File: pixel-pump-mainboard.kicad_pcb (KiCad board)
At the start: 4 copper layers, 68 x 67.3 mm, 134 parts, among them J1 JST NC Valve, J10 BM10B-SRSS-TB(LF)(SN), J11 UART/SWD DNP, J12 TYPE-C-31-M-12, J2 JST NO Valve, J3 6P4C, J4 JST 3 Way Valve, J5 Jack-DC 12V, J6 Power Sw, J7 EXP1, J8 EXP2, J9 BM04B-SRSS-TBT(LF)(SN), Q1 BSS138, Q2 BSS138, Q3 BSS138, Q4 STN4NF20L, Q5 BSS138, SW1 BOOTSEL, U1 LD1117S33TR, U2 TPS62112RSAR, U3 W25Q128JVPIQ, U4 RP2040, Y1 ABMM2-12.000MHZ-E2-T

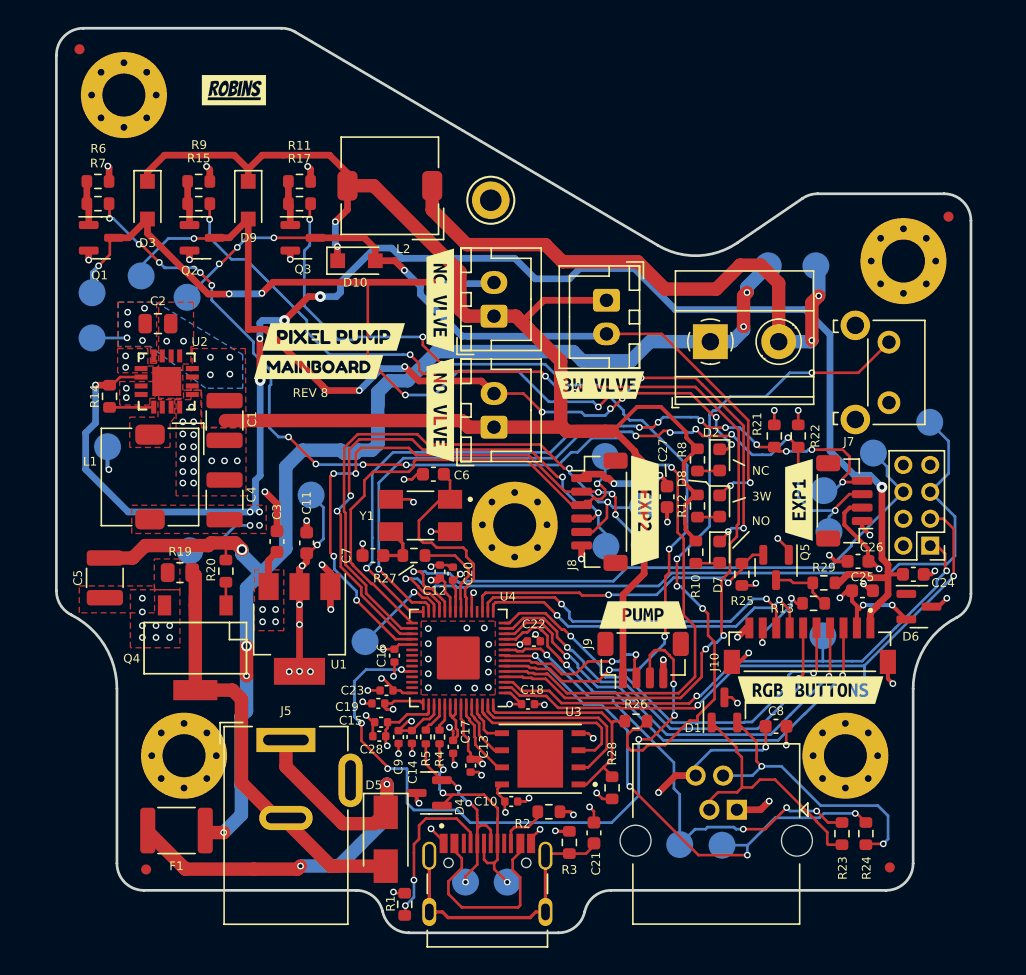
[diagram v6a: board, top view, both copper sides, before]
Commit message: Add Aisler Bridge marks
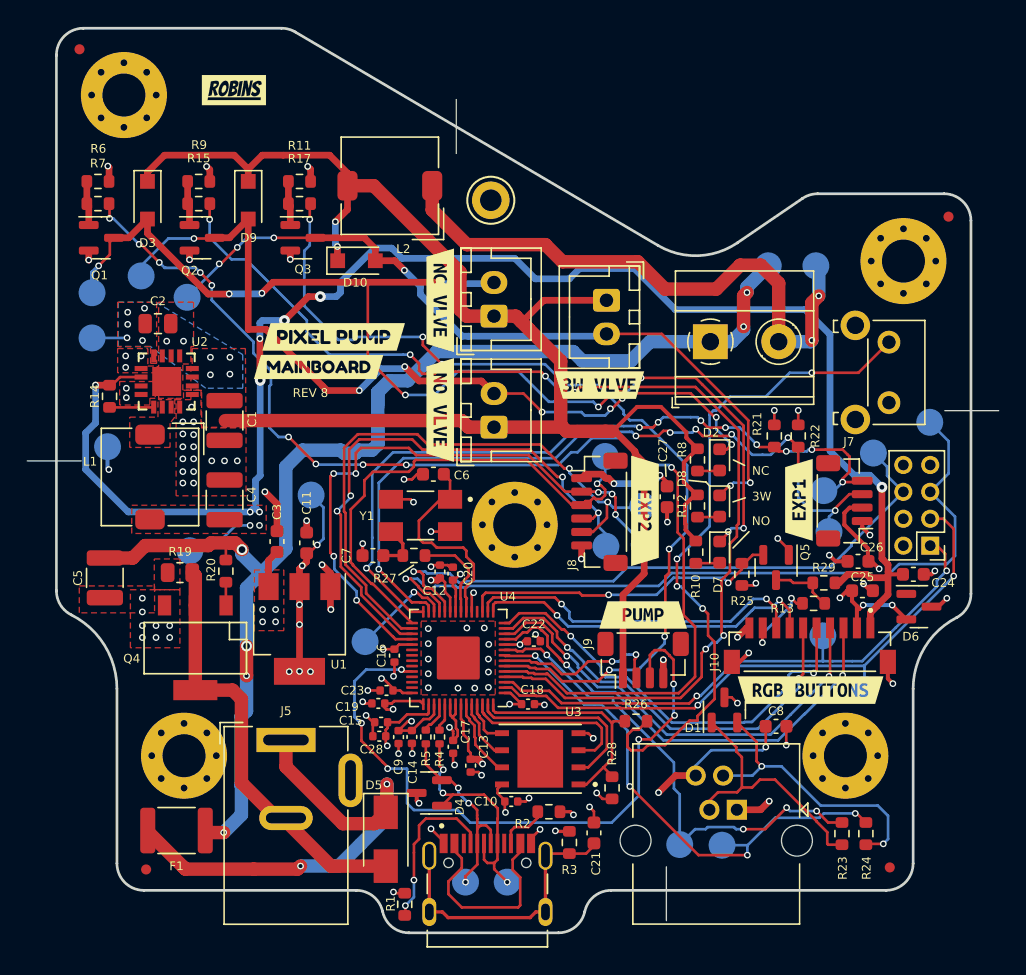
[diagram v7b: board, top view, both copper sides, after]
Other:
- board size 68 x 67.3 mm -> 72.2 x 67.3 mm
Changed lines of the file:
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@@
   (gr_line (start 92.210564 157.59322) (end 103.329656 157.59322) (layer "Edge.Cuts") (width 0.2))
   (gr_arc (start 82.739452 90.3336) (mid 83.265052 90.403899) (end 83.753702 90.609855) (layer "Edge.Cuts") (width 0.2))
+  (gr_line (start 63.8302 122.5042) (end 67.8434 122.5042) (layer "Edge.Cuts") (width 0.05))
   (gr_arc (start 121.475992 102.987506) (mid 122.013008 102.728973) (end 122.602363 102.640167) (layer "Edge.Cuts") (width 0.2))
   (gr_arc (start 72.5 154.434856) (mid 71.085786 153.84907) (end 70.5 152.434856) (layer "Edge.Cuts") (width 0.2))
@@
   (gr_line (start 132 102.640167) (end 122.602363 102.640167) (layer "Edge.Cuts") (width 0.2))
   (gr_arc (start 105.284883 156.014038) (mid 105.983455 154.878958) (end 107.24011 154.434856) (layer "Edge.Cuts") (width 0.2))
+  (gr_line (start 95.7326 99.6442) (end 95.7326 95.631) (layer "Edge.Cuts") (width 0.05))
   (gr_line (start 72.5 154.434856) (end 88.30011 154.434856) (layer "Edge.Cuts") (width 0.2))
   (gr_arc (start 134 132.387559) (mid 133.708285 133.427636) (end 132.918238 134.164307) (layer "Edge.Cuts") (width 0.2))
   (gr_arc (start 92.210564 157.59322) (mid 90.953909 157.149118) (end 90.255337 156.014038) (layer "Edge.Cuts") (width 0.2))
   (gr_arc (start 67.104294 133.951376) (mid 66.298322 133.214015) (end 66 132.163161) (layer "Edge.Cuts") (width 0.2))
+  (gr_line (start 111.3536 156.6926) (end 111.3536 152.6794) (layer "Edge.Cuts") (width 0.05))
   (gr_line (start 134 132.387558) (end 134 104.640167) (layer "Edge.Cuts") (width 0.2))
   (gr_arc (start 116.62628 106.292828) (mid 113.711299 107.244981) (end 110.739573 106.48831) (layer "Edge.Cuts") (width 0.2))
@@
   (gr_line (start 82.739452 90.333601) (end 68 90.333601) (layer "Edge.Cuts") (width 0.2))
   (gr_line (start 110.739573 106.48831) (end 83.753702 90.609855) (layer "Edge.Cuts") (width 0.2))
+  (gr_line (start 132.0546 118.7704) (end 136.0678 118.7704) (layer "Edge.Cuts") (width 0.05))
   (gr_arc (start 67.104294 133.951375) (mid 69.582658 136.218759) (end 70.5 139.450136) (layer "Edge.Cuts") (width 0.2))
   (gr_arc (start 129.699999 152.434855) (mid 129.114213 153.849069) (end 127.7 154.434856) (layer "Edge.Cuts") (width 0.2))
